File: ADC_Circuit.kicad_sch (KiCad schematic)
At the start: 53 parts, among them IC1 ADC10D040CIVS_NOPB, IC2 AD8137YRZ-REEL, IC3 AD8137YRZ-REEL, J13 Conn_01x03_Pin, J14 Conn_01x03_Pin, J4 SMA Connector, J5 SMA Connector

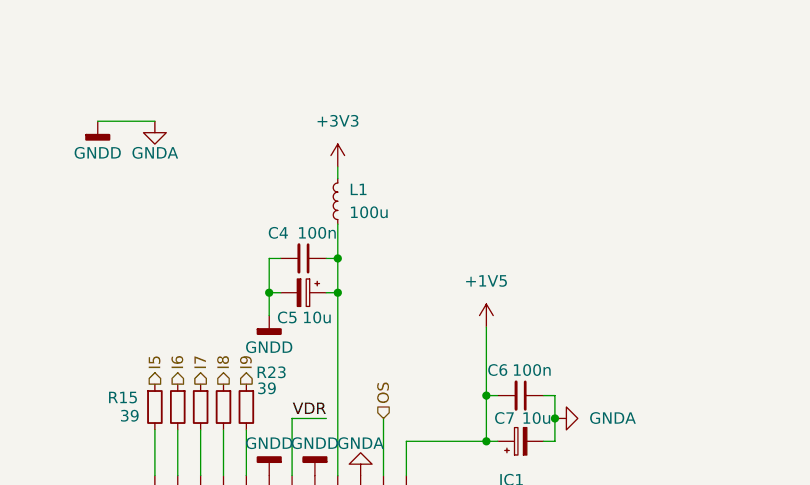
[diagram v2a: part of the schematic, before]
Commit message: Changed clock comparators to dedicated LVDS decoders and changed ADC Vdd inductor to ferrite bead
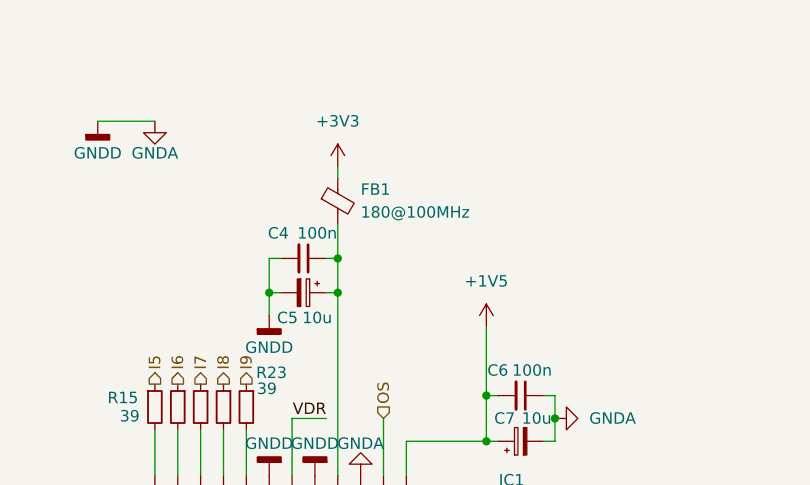
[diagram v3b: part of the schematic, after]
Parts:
- removed L1: 100u, Inductor_SMD:L_0805_2012Metric_Pad1.05x1.20mm_HandSolder, symbol Device:L_Small
- added FB1: 180@100MHz, Inductor_SMD:L_0805_2012Metric_Pad1.15x1.40mm_HandSolder, symbol Device:FerriteBead_Small
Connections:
- net +3V3: now also FB1.1
- net at C4.1, C5.1, IC1.4 (VD): now also FB1.2
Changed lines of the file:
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@@
+	)
+	(symbol
+		(lib_id "Device:FerriteBead_Small")
+		(at 85.09 39.37 0)
+		(unit 1)
+		(exclude_from_sim no)
+		(in_bom yes)
+		(on_board yes)
+		(dnp no)
+		(fields_autoplaced yes)
+		(property "Reference" "FB1"
+			(at 87.63 38.0618 0)
+			(effects
+				(font
+					(size 1.27 1.27)
+				)
+				(justify left)
+			)
+		)
+		(property "Value" "180@100MHz"
+			(at 87.63 40.6018 0)
+			(effects
+				(font
+					(size 1.27 1.27)
+				)
+				(justify left)
+			)
+		)
+		(property "Footprint" "Inductor_SMD:L_0805_2012Metric_Pad1.15x1.40mm_HandSolder"
+			(at 83.312 39.37 90)
+			(effects
+				(font
+					(size 1.27 1.27)
+				)
+				(hide yes)
+			)
+		)
+		(property "Datasheet" "~"
+			(at 85.09 39.37 0)
+			(effects
+				(font
+					(size 1.27 1.27)
+				)
+				(hide yes)
+			)
+		)
+		(property "Description" "Ferrite bead, small symbol"
+			(at 85.09 39.37 0)
+			(effects
+				(font
+					(size 1.27 1.27)
+				)
+				(hide yes)
+			)
+		)
+		(property "Mouser Link" "https://ro.mouser.com/ProductDetail/Bussmann-Eaton/MFBW1V2012-181-R?qs=W%2FMpXkg%252BdQ4AioCPKwS0Yw%3D%3D"
+			(at 85.09 39.37 0)
+			(effects
+				(font
+					(size 1.27 1.27)
+				)
+				(hide yes)
+			)
+		)
+		(pin "2"
+		)
+		(pin "1"
+		)
+		(instances
+			(project "ML605_LPC_Board_wADC_DAC"
+				(path "/35bdcd8d-8b21-4a24-9357-7d92e5ad0993/85e4bdc2-b4ea-4f24-a150-cf52be063bdc"
+					(reference "FB1")
+					(unit 1)
+				)
+			)
+		)
 	)
 	(symbol
@@
 					(unit 1)
 				)
-			)
-		)
-	)
-	(symbol
-		(lib_id "Device:L_Small")
-		(at 85.09 39.37 0)
-		(mirror y)
-		(unit 1)
-		(exclude_from_sim no)
-		(in_bom yes)
-		(on_board yes)
-		(dnp no)
-		(property "Reference" "L1"
-			(at 86.36 38.0999 0)
-			(effects
-				(font
-					(size 1.27 1.27)
-				)
-				(justify right)
-			)
-		)
-		(property "Value" "100u"
-			(at 86.36 40.6399 0)
-			(effects
-				(font
-					(size 1.27 1.27)
-				)
-				(justify right)
-			)
-		)
-		(property "Footprint" "Inductor_SMD:L_0805_2012Metric_Pad1.05x1.20mm_HandSolder"
-			(at 85.09 39.37 0)
-			(effects
-				(font
-					(size 1.27 1.27)
-				)
-				(hide yes)
-			)
-		)
-		(property "Datasheet" "~"
-			(at 85.09 39.37 0)
-			(effects
-				(font
-					(size 1.27 1.27)
-				)
-				(hide yes)
-			)
-		)
-		(property "Description" "Inductor, small symbol"
-			(at 85.09 39.37 0)
-			(effects
-				(font
-					(size 1.27 1.27)
-				)
-				(hide yes)
-			)
-		)
-		(property "Mouser Link" "https://ro.mouser.com/ProductDetail/TAIYO-YUDEN/LBR2012T101K?qs=PzICbMaShUfAbJzk8mcUcA%3D%3D"
-			(at 85.09 39.37 0)
-			(effects
-				(font
-					(size 1.27 1.27)
-				)
-				(hide yes)
-			)
-		)
-		(property "LCSC" ""
-			(at 85.09 39.37 0)
-			(effects
-				(font
-					(size 1.27 1.27)
-				)
-				(hide yes)
-			)
-		)
-		(pin "2"
-		)
-		(pin "1"
-		)
-		(instances
-			(project "ML605_LPC_Board_wADC_DAC"
-				(path "/35bdcd8d-8b21-4a24-9357-7d92e5ad0993/85e4bdc2-b4ea-4f24-a150-cf52be063bdc"
-					(reference "L1")
-					(unit 1)
-				)
